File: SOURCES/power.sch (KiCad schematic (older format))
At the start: 11 parts, among them J1 CONN_01X02

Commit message: Updated schematics
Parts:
- added FB?: 330, fdsp_capacitor:C_0805_HandSoldering, symbol FILTER
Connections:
- net VIN: now also FB?.1; no longer Cin1.1, LM1.4 (SHDN), LM1.5 (Vin)
- new net: Cin1.1, FB?.2, LM1.4 (SHDN), LM1.5 (Vin)
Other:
- moved on the sheet: Cin1
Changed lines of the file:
@@
 L C Cin1
 U 1 1 592AEB22
-P 3900 4900
-F 0 "Cin1" H 3925 5000 50  0000 L CNN
-F 1 "1u" H 3925 4800 50  0000 L CNN
-F 2 "fdsp_capacitor:C_1206_HandSoldering" H 3938 4750 30  0001 C CNN
-F 3 "" H 3900 4900 60  0000 C CNN
-	1    3900 4900
-	1    0    0    -1
-$EndComp
-Wire Wire Line
-	4850 4400 4550 4400
-Wire Wire Line
-	4550 4400 4550 4250
-Connection ~ 4550 4250
-Wire Wire Line
-	4850 4550 4850 5350
-Wire Wire Line
-	3900 5050 3900 5350
+P 4350 4900
+F 0 "Cin1" H 4375 5000 50  0000 L CNN
+F 1 "1u" H 4375 4800 50  0000 L CNN
+F 2 "fdsp_capacitor:C_1206_HandSoldering" H 4388 4750 30  0001 C CNN
+F 3 "" H 4350 4900 60  0000 C CNN
+	1    4350 4900
+	1    0    0    -1
+$EndComp
 $Comp
 L C Cboot1
@@
 	1    0    0    -1
 $EndComp
-Wire Wire Line
-	5850 4250 6350 4250
-Wire Wire Line
-	7050 4250 7050 4400
-Wire Wire Line
-	7050 4400 5850 4400
-Wire Wire Line
-	7050 4250 6650 4250
-Wire Wire Line
-	6300 4700 6300 4400
-Connection ~ 6300 4400
-Wire Wire Line
-	8200 4500 8200 4400
-Wire Wire Line
-	7650 4400 8750 4400
-Wire Wire Line
-	8200 4800 8200 4950
-Wire Wire Line
-	8750 4400 8750 4650
-Connection ~ 8200 4400
-Wire Wire Line
-	6900 4900 8200 4900
-Wire Wire Line
-	6900 4900 6900 4550
-Wire Wire Line
-	6900 4550 5850 4550
-Connection ~ 8200 4900
 $Comp
 L GND #PWR01
@@
 	1    0    0    -1
 $EndComp
-Wire Wire Line
-	5900 5450 5900 5350
-Wire Wire Line
-	1950 5350 8750 5350
-Wire Wire Line
-	8200 5350 8200 5250
-Wire Wire Line
-	8750 5350 8750 4950
-Connection ~ 8200 5350
-Wire Wire Line
-	6300 5000 6300 5350
-Connection ~ 6300 5350
-Connection ~ 5900 5350
-Connection ~ 4850 5350
 $Comp
 L VIN #PWR02
@@
 	1    0    0    -1
 $EndComp
-Wire Wire Line
-	3900 4750 3900 4250
-Connection ~ 3900 4250
-Wire Wire Line
-	2750 4250 4850 4250
 $Comp
 L BAS40-00 D3
@@
 	-1   0    0    1
 $EndComp
+$Comp
+L FILTER FB?
+U 1 1 592C3762
+P 3975 4250
+F 0 "FB?" H 3975 4400 50  0000 C CNN
+F 1 "330" H 3975 4150 50  0000 C CNN
+F 2 "fdsp_capacitor:C_0805_HandSoldering" H 3975 4250 50  0001 C CNN
+F 3 "http://www.mouser.com/ds/2/281/c31e-794748.pdf" H 3975 4250 50  0001 C CNN
+	1    3975 4250
+	1    0    0    -1
+$EndComp
+Wire Wire Line
+	4850 4400 4550 4400
+Wire Wire Line
+	4550 4400 4550 4250
+Connection ~ 4550 4250
+Wire Wire Line
+	4850 4550 4850 5350
+Wire Wire Line
+	5850 4250 6350 4250
+Wire Wire Line
+	7050 4250 7050 4400
+Wire Wire Line
+	7050 4400 5850 4400
+Wire Wire Line
+	7050 4250 6650 4250
+Wire Wire Line
+	6300 4700 6300 4400
+Connection ~ 6300 4400
+Wire Wire Line
+	8200 4500 8200 4400
+Wire Wire Line
+	7650 4400 8750 4400
+Wire Wire Line
+	8200 4800 8200 4950
+Wire Wire Line
+	8750 4400 8750 4650
+Connection ~ 8200 4400
+Wire Wire Line
+	6900 4900 8200 4900
+Wire Wire Line
+	6900 4900 6900 4550
+Wire Wire Line
+	6900 4550 5850 4550
+Connection ~ 8200 4900
+Wire Wire Line
+	5900 5450 5900 5350
+Wire Wire Line
+	1950 5350 8750 5350
+Wire Wire Line
+	8200 5350 8200 5250
+Wire Wire Line
+	8750 5350 8750 4950
+Connection ~ 8200 5350
+Wire Wire Line
+	6300 5000 6300 5350
+Connection ~ 6300 5350
+Connection ~ 5900 5350
+Connection ~ 4850 5350
 Wire Wire Line
 	1950 5350 1950 4350
-Connection ~ 3900 5350
 Wire Wire Line
 	3100 5100 3100 5350
@@
 	3100 4700 3100 4250
 Connection ~ 3100 4250
+Wire Wire Line
+	2750 4250 3625 4250
+Wire Wire Line
+	4325 4250 4850 4250
+Wire Wire Line
+	4350 4750 4350 4250
+Connection ~ 4350 4250
+Wire Wire Line
+	4350 5050 4350 5350
+Connection ~ 4350 5350
 $EndSCHEMATC

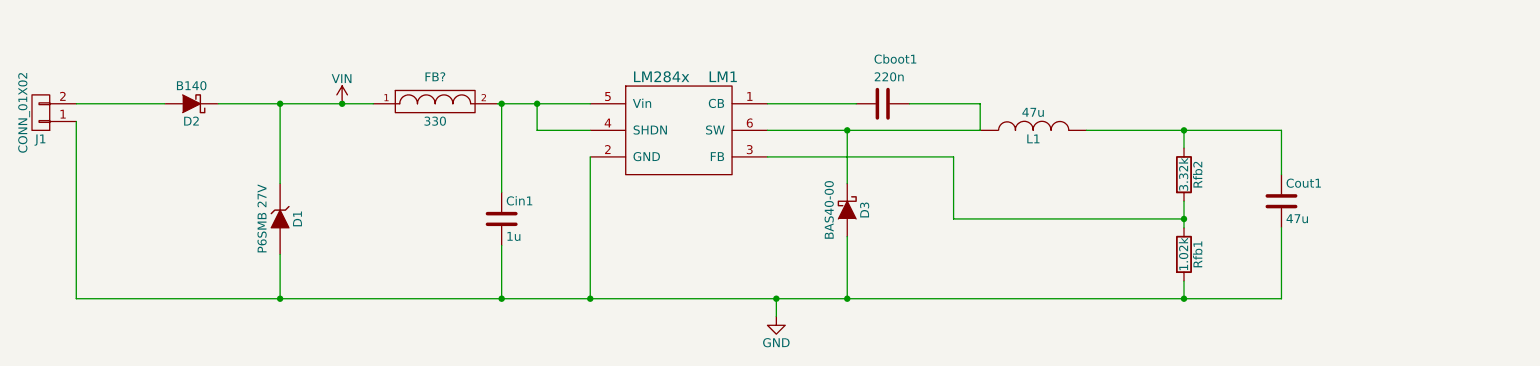
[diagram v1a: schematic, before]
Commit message: Updated schematics and labels
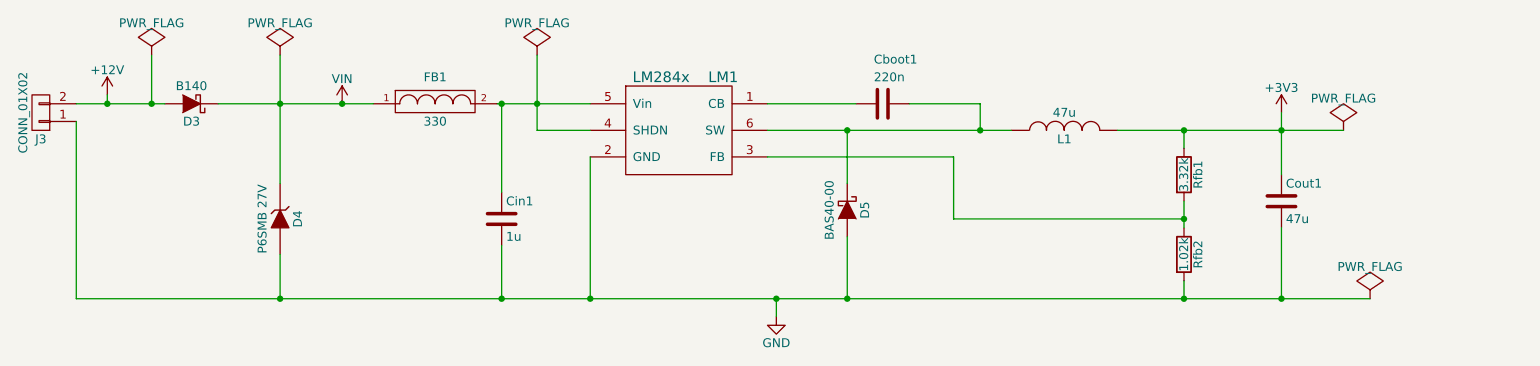
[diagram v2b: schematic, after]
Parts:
- gave numbers to parts that had none: 1
- renumbered D2 to D3, D1 to D4, D3 to D5, J1 to J3, Rfb2 to Rfb1, Rfb1 to Rfb2
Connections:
- net +3V3: now reaches Cout1.1, L1.2, Rfb1.1
- net +12V: now reaches D3.2 (A), J3.2 (P2)
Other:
- moved on the sheet: L1
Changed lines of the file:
@@
 L L L1
 U 1 1 592AEE35
-P 7350 4400
-F 0 "L1" V 7300 4400 50  0000 C CNN
-F 1 "47u" V 7450 4400 50  0000 C CNN
-F 2 "power_lib:Choke_SMD_6.0x5.8" H 7350 4400 60  0001 C CNN
-F 3 "" H 7350 4400 60  0000 C CNN
-	1    7350 4400
+P 7525 4400
+F 0 "L1" V 7475 4400 50  0000 C CNN
+F 1 "47u" V 7625 4400 50  0000 C CNN
+F 2 "power_lib:Choke_SMD_6.0x5.8" H 7525 4400 60  0001 C CNN
+F 3 "" H 7525 4400 60  0000 C CNN
+	1    7525 4400
 	0    -1   -1   0
 $EndComp
 $Comp
-L R Rfb2
+L R Rfb1
 U 1 1 592AF0E0
 P 8200 4650
-F 0 "Rfb2" V 8280 4650 50  0000 C CNN
+F 0 "Rfb1" V 8280 4650 50  0000 C CNN
 F 1 "3.32k" V 8200 4650 50  0000 C CNN
 F 2 "fdsp_resistor:R_1206_HandSoldering" V 8130 4650 30  0001 C CNN
@@
 $EndComp
 $Comp
-L R Rfb1
+L R Rfb2
 U 1 1 592AF16B
 P 8200 5100
-F 0 "Rfb1" V 8280 5100 50  0000 C CNN
+F 0 "Rfb2" V 8280 5100 50  0000 C CNN
 F 1 "1.02k" V 8200 5100 50  0000 C CNN
 F 2 "fdsp_resistor:R_1206_HandSoldering" V 8130 5100 30  0001 C CNN
@@
 $EndComp
 $Comp
-L GND #PWR01
+L GND #PWR066
 U 1 1 592AF8ED
 P 5900 5450
-F 0 "#PWR01" H 5900 5200 50  0001 C CNN
+F 0 "#PWR066" H 5900 5200 50  0001 C CNN
 F 1 "GND" H 5900 5300 50  0000 C CNN
 F 2 "" H 5900 5450 60  0000 C CNN
@@
 $EndComp
 $Comp
-L VIN #PWR02
+L VIN #PWR067
 U 1 1 592B0082
 P 3450 4250
-F 0 "#PWR02" H 3450 4100 50  0001 C CNN
+F 0 "#PWR067" H 3450 4100 50  0001 C CNN
 F 1 "VIN" H 3450 4390 50  0000 C CNN
 F 2 "" H 3450 4250 60  0000 C CNN
@@
 $EndComp
 $Comp
-L BAS40-00 D3
+L BAS40-00 D5
 U 1 1 592B508F
 P 6300 4850
-F 0 "D3" H 6300 4950 50  0000 C CNN
+F 0 "D5" H 6300 4950 50  0000 C CNN
 F 1 "BAS40-00" H 6300 4750 50  0000 C CNN
 F 2 "TO_SOT_Packages_SMD:SOT-23" H 6300 4650 20  0001 C CNN
@@
 $EndComp
 $Comp
-L ZENER D1
+L ZENER D4
 U 1 1 592B0AB6
 P 3100 4900
-F 0 "D1" H 3100 5000 50  0000 C CNN
+F 0 "D4" H 3100 5000 50  0000 C CNN
 F 1 "P6SMB 27V" H 3100 4800 50  0000 C CNN
 F 2 "fdsp_diode:SMB" H 3100 4900 60  0001 C CNN
@@
 $EndComp
 $Comp
-L D_Schottky D2
+L D_Schottky D3
 U 1 1 592B0C13
 P 2600 4250
-F 0 "D2" H 2600 4350 50  0000 C CNN
+F 0 "D3" H 2600 4350 50  0000 C CNN
 F 1 "B140" H 2600 4150 50  0000 C CNN
 F 2 "fdsp_diode:SMA" H 2600 4250 60  0001 C CNN
@@
 $EndComp
 $Comp
-L CONN_01X02 J1
+L CONN_01X02 J3
 U 1 1 592B0D49
 P 1750 4300
-F 0 "J1" H 1750 4450 50  0000 C CNN
+F 0 "J3" H 1750 4450 50  0000 C CNN
 F 1 "CONN_01X02" V 1850 4300 50  0000 C CNN
 F 2 "fdsp_connector:RIACON101-2" H 1750 4300 50  0001 C CNN
@@
 $EndComp
 $Comp
-L FILTER FB?
+L FILTER FB1
 U 1 1 592C3762
 P 3975 4250
-F 0 "FB?" H 3975 4400 50  0000 C CNN
+F 0 "FB1" H 3975 4400 50  0000 C CNN
 F 1 "330" H 3975 4150 50  0000 C CNN
 F 2 "fdsp_capacitor:C_0805_HandSoldering" H 3975 4250 50  0001 C CNN
@@
 $EndComp
 Wire Wire Line
-	4850 4400 4550 4400
-Wire Wire Line
-	4550 4400 4550 4250
+	4550 4400 4850 4400
+Wire Wire Line
+	4550 3975 4550 4400
 Connection ~ 4550 4250
 Wire Wire Line
@@
 	7050 4250 7050 4400
 Wire Wire Line
-	7050 4400 5850 4400
+	5850 4400 7225 4400
 Wire Wire Line
 	7050 4250 6650 4250
@@
 	8200 4500 8200 4400
 Wire Wire Line
-	7650 4400 8750 4400
-Wire Wire Line
 	8200 4800 8200 4950
 Wire Wire Line
-	8750 4400 8750 4650
+	8750 4300 8750 4650
 Connection ~ 8200 4400
 Wire Wire Line
@@
 	5900 5450 5900 5350
 Wire Wire Line
-	1950 5350 8750 5350
+	1950 5350 9250 5350
 Wire Wire Line
 	8200 5350 8200 5250
@@
 Connection ~ 3450 4250
 Wire Wire Line
-	3100 4700 3100 4250
+	3100 3975 3100 4700
 Connection ~ 3100 4250
 Wire Wire Line
@@
 	4350 5050 4350 5350
 Connection ~ 4350 5350
+$Comp
+L +12V #PWR068
+U 1 1 592E15F4
+P 2125 4200
+F 0 "#PWR068" H 2125 4050 50  0001 C CNN
+F 1 "+12V" H 2125 4340 50  0000 C CNN
+F 2 "" H 2125 4200 60  0000 C CNN
+F 3 "" H 2125 4200 60  0000 C CNN
+	1    2125 4200
+	1    0    0    -1
+$EndComp
+Connection ~ 7050 4400
+Wire Wire Line
+	7825 4400 9100 4400
+Connection ~ 8750 4400
+$Comp
+L +3V3 #PWR069
+U 1 1 592E1EE2
+P 8750 4300
+F 0 "#PWR069" H 8750 4150 50  0001 C CNN
+F 1 "+3V3" H 8750 4440 50  0000 C CNN
+F 2 "" H 8750 4300 60  0000 C CNN
+F 3 "" H 8750 4300 60  0000 C CNN
+	1    8750 4300
+	1    0    0    -1
+$EndComp
+$Comp
+L PWR_FLAG #FLG070
+U 1 1 5932FFE3
+P 9100 4400
+F 0 "#FLG070" H 9100 4495 50  0001 C CNN
+F 1 "PWR_FLAG" H 9100 4580 50  0000 C CNN
+F 2 "" H 9100 4400 50  0000 C CNN
+F 3 "" H 9100 4400 50  0000 C CNN
+	1    9100 4400
+	1    0    0    -1
+$EndComp
+$Comp
+L PWR_FLAG #FLG071
+U 1 1 59330168
+P 9250 5350
+F 0 "#FLG071" H 9250 5445 50  0001 C CNN
+F 1 "PWR_FLAG" H 9250 5530 50  0000 C CNN
+F 2 "" H 9250 5350 50  0000 C CNN
+F 3 "" H 9250 5350 50  0000 C CNN
+	1    9250 5350
+	1    0    0    -1
+$EndComp
+Connection ~ 8750 5350
+$Comp
+L PWR_FLAG #FLG072
+U 1 1 59330402
+P 2375 3975
+F 0 "#FLG072" H 2375 4070 50  0001 C CNN
+F 1 "PWR_FLAG" H 2375 4155 50  0000 C CNN
+F 2 "" H 2375 3975 50  0000 C CNN
+F 3 "" H 2375 3975 50  0000 C CNN
+	1    2375 3975
+	1    0    0    -1
+$EndComp
+$Comp
+L PWR_FLAG #FLG073
+U 1 1 59330444
+P 3100 3975
+F 0 "#FLG073" H 3100 4070 50  0001 C CNN
+F 1 "PWR_FLAG" H 3100 4155 50  0000 C CNN
+F 2 "" H 3100 3975 50  0000 C CNN
+F 3 "" H 3100 3975 50  0000 C CNN
+	1    3100 3975
+	1    0    0    -1
+$EndComp
+Wire Wire Line
+	2375 3975 2375 4250
+Connection ~ 2375 4250
+$Comp
+L PWR_FLAG #FLG074
+U 1 1 593306EC
+P 4550 3975
+F 0 "#FLG074" H 4550 4070 50  0001 C CNN
+F 1 "PWR_FLAG" H 4550 4155 50  0000 C CNN
+F 2 "" H 4550 3975 50  0000 C CNN
+F 3 "" H 4550 3975 50  0000 C CNN
+	1    4550 3975
+	1    0    0    -1
+$EndComp
+Wire Wire Line
+	2125 4200 2125 4250
+Connection ~ 2125 4250
 $EndSCHEMATC

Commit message: Assigned footprints
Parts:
- Cin1: value 1u -> 2u2
- D3: value B140 -> B150
- D5: value BAS40-00 -> B150; footprint TO_SOT_Packages_SMD:SOT-23 -> fdsp_diode:SMA
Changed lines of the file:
@@
 P 4350 4900
 F 0 "Cin1" H 4375 5000 50  0000 L CNN
-F 1 "1u" H 4375 4800 50  0000 L CNN
+F 1 "2u2" H 4375 4800 50  0000 L CNN
 F 2 "fdsp_capacitor:C_1206_HandSoldering" H 4388 4750 30  0001 C CNN
 F 3 "" H 4350 4900 60  0000 C CNN
@@
 $EndComp
 $Comp
-L GND #PWR066
+L GND #PWR065
 U 1 1 592AF8ED
 P 5900 5450
-F 0 "#PWR066" H 5900 5200 50  0001 C CNN
+F 0 "#PWR065" H 5900 5200 50  0001 C CNN
 F 1 "GND" H 5900 5300 50  0000 C CNN
 F 2 "" H 5900 5450 60  0000 C CNN
@@
 $EndComp
 $Comp
-L VIN #PWR067
+L VIN #PWR066
 U 1 1 592B0082
 P 3450 4250
-F 0 "#PWR067" H 3450 4100 50  0001 C CNN
+F 0 "#PWR066" H 3450 4100 50  0001 C CNN
 F 1 "VIN" H 3450 4390 50  0000 C CNN
 F 2 "" H 3450 4250 60  0000 C CNN
@@
 P 6300 4850
 F 0 "D5" H 6300 4950 50  0000 C CNN
-F 1 "BAS40-00" H 6300 4750 50  0000 C CNN
-F 2 "TO_SOT_Packages_SMD:SOT-23" H 6300 4650 20  0001 C CNN
-F 3 "http://www.vishay.com/docs/85701/bas40v.pdf" H 6300 4700 20  0001 C CNN
+F 1 "B150" H 6300 4750 50  0000 C CNN
+F 2 "fdsp_diode:SMA" H 6300 4650 20  0001 C CNN
+F 3 "hhttp://www.mouser.com/ds/2/115/ds13002-60388.pdf" H 6300 4700 20  0001 C CNN
 	1    6300 4850
 	0    1    1    0
@@
 P 2600 4250
 F 0 "D3" H 2600 4350 50  0000 C CNN
-F 1 "B140" H 2600 4150 50  0000 C CNN
+F 1 "B150" H 2600 4150 50  0000 C CNN
 F 2 "fdsp_diode:SMA" H 2600 4250 60  0001 C CNN
 F 3 "http://www.mouser.com/ds/2/115/ds13002-60388.pdf" H 2600 4250 60  0001 C CNN
@@
 	5900 5450 5900 5350
 Wire Wire Line
-	1950 5350 9250 5350
-Wire Wire Line
 	8200 5350 8200 5250
 Wire Wire Line
@@
 Connection ~ 4350 5350
 $Comp
-L +12V #PWR068
+L +12V #PWR067
 U 1 1 592E15F4
 P 2125 4200
-F 0 "#PWR068" H 2125 4050 50  0001 C CNN
+F 0 "#PWR067" H 2125 4050 50  0001 C CNN
 F 1 "+12V" H 2125 4340 50  0000 C CNN
 F 2 "" H 2125 4200 60  0000 C CNN
@@
 Connection ~ 8750 4400
 $Comp
-L +3V3 #PWR069
+L +3V3 #PWR068
 U 1 1 592E1EE2
 P 8750 4300
-F 0 "#PWR069" H 8750 4150 50  0001 C CNN
+F 0 "#PWR068" H 8750 4150 50  0001 C CNN
 F 1 "+3V3" H 8750 4440 50  0000 C CNN
 F 2 "" H 8750 4300 60  0000 C CNN
@@
 $EndComp
 $Comp
-L PWR_FLAG #FLG070
+L PWR_FLAG #FLG069
 U 1 1 5932FFE3
 P 9100 4400
-F 0 "#FLG070" H 9100 4495 50  0001 C CNN
+F 0 "#FLG069" H 9100 4495 50  0001 C CNN
 F 1 "PWR_FLAG" H 9100 4580 50  0000 C CNN
 F 2 "" H 9100 4400 50  0000 C CNN
@@
 	1    0    0    -1
 $EndComp
-$Comp
-L PWR_FLAG #FLG071
-U 1 1 59330168
-P 9250 5350
-F 0 "#FLG071" H 9250 5445 50  0001 C CNN
-F 1 "PWR_FLAG" H 9250 5530 50  0000 C CNN
-F 2 "" H 9250 5350 50  0000 C CNN
-F 3 "" H 9250 5350 50  0000 C CNN
-	1    9250 5350
-	1    0    0    -1
-$EndComp
 Connection ~ 8750 5350
 $Comp
-L PWR_FLAG #FLG072
+L PWR_FLAG #FLG070
 U 1 1 59330402
 P 2375 3975
-F 0 "#FLG072" H 2375 4070 50  0001 C CNN
+F 0 "#FLG070" H 2375 4070 50  0001 C CNN
 F 1 "PWR_FLAG" H 2375 4155 50  0000 C CNN
 F 2 "" H 2375 3975 50  0000 C CNN
@@
 $EndComp
 $Comp
-L PWR_FLAG #FLG073
+L PWR_FLAG #FLG071
 U 1 1 59330444
 P 3100 3975
-F 0 "#FLG073" H 3100 4070 50  0001 C CNN
+F 0 "#FLG071" H 3100 4070 50  0001 C CNN
 F 1 "PWR_FLAG" H 3100 4155 50  0000 C CNN
 F 2 "" H 3100 3975 50  0000 C CNN
@@
 Connection ~ 2375 4250
 $Comp
-L PWR_FLAG #FLG074
+L PWR_FLAG #FLG072
 U 1 1 593306EC
 P 4550 3975
-F 0 "#FLG074" H 4550 4070 50  0001 C CNN
+F 0 "#FLG072" H 4550 4070 50  0001 C CNN
 F 1 "PWR_FLAG" H 4550 4155 50  0000 C CNN
 F 2 "" H 4550 3975 50  0000 C CNN
@@
 	2125 4200 2125 4250
 Connection ~ 2125 4250
+Wire Wire Line
+	1950 5350 8750 5350
 $EndSCHEMATC

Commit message: updated schematic + bom + pcb start
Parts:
- removed D5: B150, fdsp_diode:SMA, symbol BAS40-00
- added C_res1, C_res3, C_res4: x, fdsp_capacitor:C_Radial_D5_L11_P2, symbol CP
- added C_res2: x, fdsp_capacitor:C_1206_HandSoldering, symbol C
- added D5: B150, fdsp_diode:SMA, symbol D_Schottky
- L1: footprint power_lib:Choke_SMD_6.0x5.8 -> fdsp_inductor_new:Choke_SMD_6.0x5.8
- LM1: symbol LM284x -> LM284x-RESCUE-freeDSP_Classic_SMD
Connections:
- net +3V3: now also C_res2.1, C_res3.1, C_res4.1
- net GND: now also C_res1.2, C_res2.2, C_res3.2, C_res4.2, D5.2 (A)
- net at Cin1.1, FB1.2, LM1.4 (SHDN)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: now also C_res1.1
- net at Cboot1.1, L1.1, LM1.6 (SW): now also D5.1 (K)
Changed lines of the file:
@@
 EESchema Schematic File Version 2
+LIBS:freeDSP_Classic_SMD-rescue
 LIBS:fdsp_device_new
 LIBS:fdsp_digital_new
@@
 $EndDescr
 $Comp
-L LM284x LM1
+L LM284x-RESCUE-freeDSP_Classic_SMD LM1
 U 1 1 592AEAF9
 P 5350 4400
@@
 F 0 "L1" V 7475 4400 50  0000 C CNN
 F 1 "47u" V 7625 4400 50  0000 C CNN
-F 2 "power_lib:Choke_SMD_6.0x5.8" H 7525 4400 60  0001 C CNN
+F 2 "fdsp_inductor_new:Choke_SMD_6.0x5.8" H 7525 4400 60  0001 C CNN
 F 3 "" H 7525 4400 60  0000 C CNN
 	1    7525 4400
@@
 $EndComp
 $Comp
-L GND #PWR065
+L GND #PWR067
 U 1 1 592AF8ED
 P 5900 5450
-F 0 "#PWR065" H 5900 5200 50  0001 C CNN
+F 0 "#PWR067" H 5900 5200 50  0001 C CNN
 F 1 "GND" H 5900 5300 50  0000 C CNN
 F 2 "" H 5900 5450 60  0000 C CNN
@@
 $EndComp
 $Comp
-L VIN #PWR066
+L VIN #PWR068
 U 1 1 592B0082
-P 3450 4250
-F 0 "#PWR066" H 3450 4100 50  0001 C CNN
-F 1 "VIN" H 3450 4390 50  0000 C CNN
-F 2 "" H 3450 4250 60  0000 C CNN
-F 3 "" H 3450 4250 60  0000 C CNN
-	1    3450 4250
-	1    0    0    -1
-$EndComp
-$Comp
-L BAS40-00 D5
-U 1 1 592B508F
-P 6300 4850
-F 0 "D5" H 6300 4950 50  0000 C CNN
-F 1 "B150" H 6300 4750 50  0000 C CNN
-F 2 "fdsp_diode:SMA" H 6300 4650 20  0001 C CNN
-F 3 "hhttp://www.mouser.com/ds/2/115/ds13002-60388.pdf" H 6300 4700 20  0001 C CNN
-	1    6300 4850
-	0    1    1    0
+P 3450 4150
+F 0 "#PWR068" H 3450 4000 50  0001 C CNN
+F 1 "VIN" H 3450 4290 50  0000 C CNN
+F 2 "" H 3450 4150 60  0000 C CNN
+F 3 "" H 3450 4150 60  0000 C CNN
+	1    3450 4150
+	1    0    0    -1
 $EndComp
 $Comp
@@
 Connection ~ 3100 4250
 Wire Wire Line
-	2750 4250 3625 4250
-Wire Wire Line
 	4325 4250 4850 4250
 Wire Wire Line
@@
 Connection ~ 4350 5350
 $Comp
-L +12V #PWR067
+L +12V #PWR069
 U 1 1 592E15F4
 P 2125 4200
-F 0 "#PWR067" H 2125 4050 50  0001 C CNN
+F 0 "#PWR069" H 2125 4050 50  0001 C CNN
 F 1 "+12V" H 2125 4340 50  0000 C CNN
 F 2 "" H 2125 4200 60  0000 C CNN
@@
 Connection ~ 7050 4400
 Wire Wire Line
-	7825 4400 9100 4400
+	7825 4400 9800 4400
 Connection ~ 8750 4400
 $Comp
-L +3V3 #PWR068
+L +3V3 #PWR070
 U 1 1 592E1EE2
 P 8750 4300
-F 0 "#PWR068" H 8750 4150 50  0001 C CNN
+F 0 "#PWR070" H 8750 4150 50  0001 C CNN
 F 1 "+3V3" H 8750 4440 50  0000 C CNN
 F 2 "" H 8750 4300 60  0000 C CNN
@@
 $EndComp
 $Comp
-L PWR_FLAG #FLG069
+L PWR_FLAG #FLG071
 U 1 1 5932FFE3
 P 9100 4400
-F 0 "#FLG069" H 9100 4495 50  0001 C CNN
+F 0 "#FLG071" H 9100 4495 50  0001 C CNN
 F 1 "PWR_FLAG" H 9100 4580 50  0000 C CNN
 F 2 "" H 9100 4400 50  0000 C CNN
@@
 Connection ~ 8750 5350
 $Comp
-L PWR_FLAG #FLG070
+L PWR_FLAG #FLG072
 U 1 1 59330402
 P 2375 3975
-F 0 "#FLG070" H 2375 4070 50  0001 C CNN
+F 0 "#FLG072" H 2375 4070 50  0001 C CNN
 F 1 "PWR_FLAG" H 2375 4155 50  0000 C CNN
 F 2 "" H 2375 3975 50  0000 C CNN
@@
 $EndComp
 $Comp
-L PWR_FLAG #FLG071
+L PWR_FLAG #FLG073
 U 1 1 59330444
 P 3100 3975
-F 0 "#FLG071" H 3100 4070 50  0001 C CNN
+F 0 "#FLG073" H 3100 4070 50  0001 C CNN
 F 1 "PWR_FLAG" H 3100 4155 50  0000 C CNN
 F 2 "" H 3100 3975 50  0000 C CNN
@@
 Connection ~ 2375 4250
 $Comp
-L PWR_FLAG #FLG072
+L PWR_FLAG #FLG074
 U 1 1 593306EC
 P 4550 3975
-F 0 "#FLG072" H 4550 4070 50  0001 C CNN
+F 0 "#FLG074" H 4550 4070 50  0001 C CNN
 F 1 "PWR_FLAG" H 4550 4155 50  0000 C CNN
 F 2 "" H 4550 3975 50  0000 C CNN
@@
 Connection ~ 2125 4250
 Wire Wire Line
-	1950 5350 8750 5350
+	1950 5350 9800 5350
+$Comp
+L CP C_res3
+U 1 1 592EFEEA
+P 9450 4800
+F 0 "C_res3" H 9475 4900 50  0000 L CNN
+F 1 "x" H 9475 4700 50  0000 L CNN
+F 2 "fdsp_capacitor:C_Radial_D5_L11_P2" H 9488 4650 30  0001 C CNN
+F 3 "" H 9450 4800 60  0000 C CNN
+	1    9450 4800
+	1    0    0    -1
+$EndComp
+$Comp
+L CP C_res4
+U 1 1 592EFFF6
+P 9800 4800
+F 0 "C_res4" H 9825 4900 50  0000 L CNN
+F 1 "x" H 9825 4700 50  0000 L CNN
+F 2 "fdsp_capacitor:C_Radial_D5_L11_P2" H 9838 4650 30  0001 C CNN
+F 3 "" H 9800 4800 60  0000 C CNN
+	1    9800 4800
+	1    0    0    -1
+$EndComp
+$Comp
+L C C_res2
+U 1 1 592F003A
+P 9100 4800
+F 0 "C_res2" H 9125 4900 50  0000 L CNN
+F 1 "x" H 9125 4700 50  0000 L CNN
+F 2 "fdsp_capacitor:C_1206_HandSoldering" H 9138 4650 30  0001 C CNN
+F 3 "" H 9100 4800 60  0000 C CNN
+	1    9100 4800
+	1    0    0    -1
+$EndComp
+Wire Wire Line
+	9800 4400 9800 4650
+Connection ~ 9100 4400
+Wire Wire Line
+	9100 4650 9100 4400
+Wire Wire Line
+	9450 4650 9450 4400
+Connection ~ 9450 4400
+Wire Wire Line
+	9100 5350 9100 4950
+Wire Wire Line
+	9450 5350 9450 4950
+Connection ~ 9100 5350
+Wire Wire Line
+	9800 5350 9800 4950
+Connection ~ 9450 5350
+$Comp
+L CP C_res1
+U 1 1 592F05A0
+P 4600 4900
+F 0 "C_res1" H 4625 5000 50  0000 L CNN
+F 1 "x" H 4625 4800 50  0000 L CNN
+F 2 "fdsp_capacitor:C_Radial_D5_L11_P2" H 4638 4750 30  0001 C CNN
+F 3 "" H 4600 4900 60  0000 C CNN
+	1    4600 4900
+	1    0    0    -1
+$EndComp
+Wire Wire Line
+	3450 4150 3450 4250
+Wire Wire Line
+	2750 4250 3625 4250
+Wire Wire Line
+	4600 4750 4600 4400
+Connection ~ 4600 4400
+Wire Wire Line
+	4600 5050 4600 5350
+Connection ~ 4600 5350
+$Comp
+L D_Schottky D5
+U 1 1 592EBAF3
+P 6300 4850
+F 0 "D5" H 6300 4950 50  0000 C CNN
+F 1 "B150" H 6300 4750 50  0000 C CNN
+F 2 "fdsp_diode:SMA" H 6300 4850 60  0001 C CNN
+F 3 "http://www.mouser.com/ds/2/115/ds13002-60388.pdf" H 6300 4850 60  0001 C CNN
+	1    6300 4850
+	0    1    1    0
+$EndComp
 $EndSCHEMATC

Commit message: updated pcb
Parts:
- removed C_res4: x, fdsp_capacitor:C_Radial_D5_L11_P2, symbol CP
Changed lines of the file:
@@
 $EndComp
 Connection ~ 7050 4400
-Wire Wire Line
-	7825 4400 9800 4400
 Connection ~ 8750 4400
 $Comp
@@
 	2125 4200 2125 4250
 Connection ~ 2125 4250
-Wire Wire Line
-	1950 5350 9800 5350
 $Comp
 L CP C_res3
@@
 F 3 "" H 9450 4800 60  0000 C CNN
 	1    9450 4800
-	1    0    0    -1
-$EndComp
-$Comp
-L CP C_res4
-U 1 1 592EFFF6
-P 9800 4800
-F 0 "C_res4" H 9825 4900 50  0000 L CNN
-F 1 "x" H 9825 4700 50  0000 L CNN
-F 2 "fdsp_capacitor:C_Radial_D5_L11_P2" H 9838 4650 30  0001 C CNN
-F 3 "" H 9800 4800 60  0000 C CNN
-	1    9800 4800
 	1    0    0    -1
 $EndComp
@@
 	1    0    0    -1
 $EndComp
-Wire Wire Line
-	9800 4400 9800 4650
 Connection ~ 9100 4400
 Wire Wire Line
 	9100 4650 9100 4400
 Wire Wire Line
-	9450 4650 9450 4400
-Connection ~ 9450 4400
+	9450 4400 9450 4650
 Wire Wire Line
 	9100 5350 9100 4950
@@
 	9450 5350 9450 4950
 Connection ~ 9100 5350
-Wire Wire Line
-	9800 5350 9800 4950
-Connection ~ 9450 5350
 $Comp
 L CP C_res1
@@
 	0    1    1    0
 $EndComp
+Wire Wire Line
+	7825 4400 9450 4400
+Wire Wire Line
+	9450 5350 1950 5350
 $EndSCHEMATC
